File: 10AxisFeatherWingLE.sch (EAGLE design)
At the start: 26 parts, among them J5 QWIIC, U1 LSM9DS1, U2 BME280

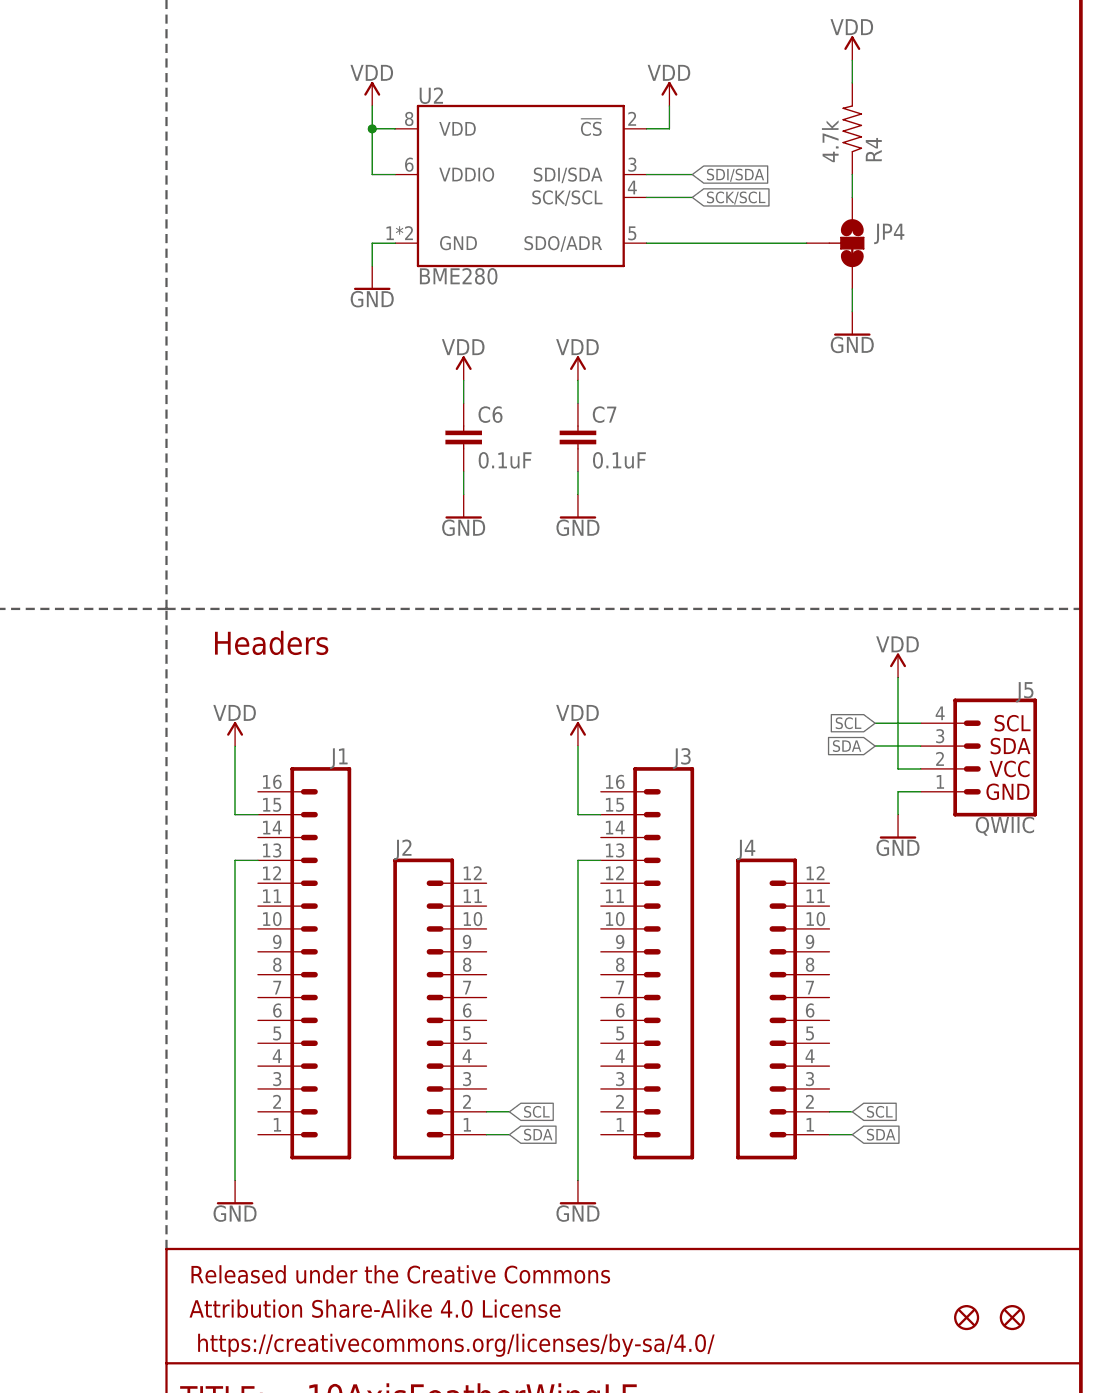
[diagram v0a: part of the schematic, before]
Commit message: Added traces
Added traces to board file.
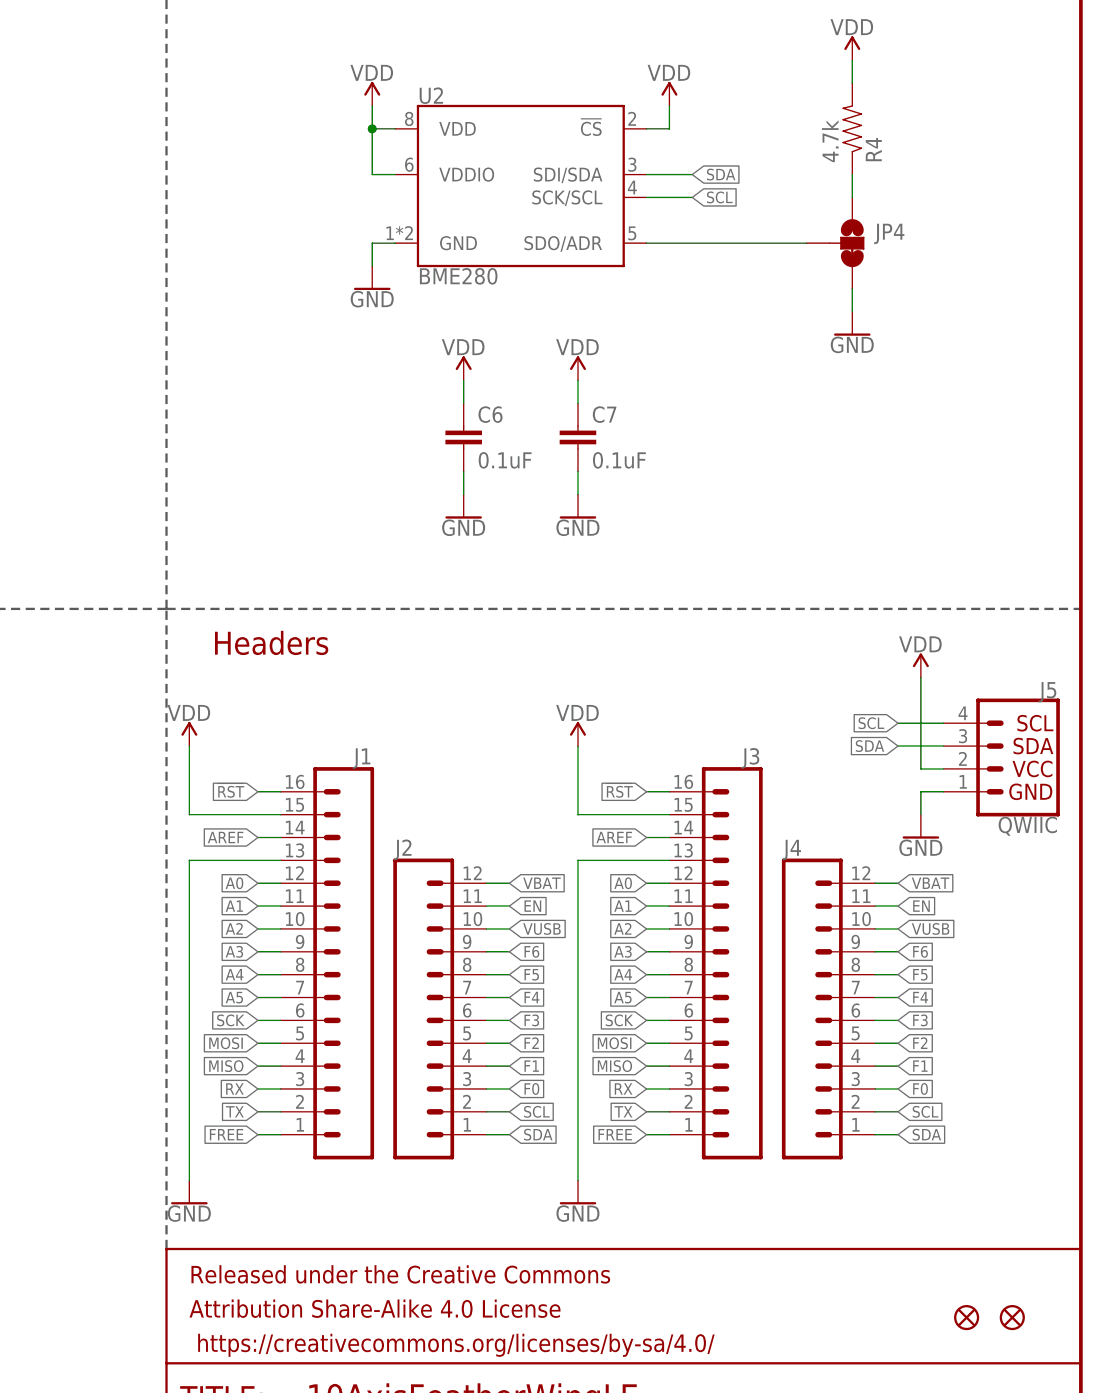
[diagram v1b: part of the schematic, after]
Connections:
- net SDO/ADR renamed SDO
- removed net SCK/SCL: U2.SCK/SCL
- removed net SDI/SDA: U2.SDI/SDA
- new net !RST: J1.16, J3.16
- new net A0: J1.12, J3.12
- new net A1: J1.11, J3.11
- new net A2: J1.10, J3.10
- new net A3: J1.9, J3.9
- new net A4: J1.8, J3.8
- new net A5: J1.7, J3.7
- new net AREF: J1.14, J3.14
- new net EN: J2.11, J4.11
- new net F0: J2.3, J4.3
- new net F1: J2.4, J4.4
- new net F2: J2.5, J4.5
- new net F3: J2.6, J4.6
- new net F4: J2.7, J4.7
- new net F5: J2.8, J4.8
- new net F6: J2.9, J4.9
- new net FREE: J1.1, J3.1
- new net MISO: J1.4, J3.4
- new net MOSI: J1.5, J3.5
- new net RX: J1.3, J3.3
- new net SCK: J1.6, J3.6
- new net TX: J1.2, J3.2
- new net VBAT: J2.12, J4.12
- new net VUSB: J2.10, J4.10
- net SCL: now also U2.SCK/SCL
- net SDA: now also U2.SDI/SDA
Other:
- moved on the sheet: J1, J3, J4, J5
